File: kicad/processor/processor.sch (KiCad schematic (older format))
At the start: 24 parts, among them J1 CONN_02X07, U1 ESP32-WROOM, U2 BME280, U3 TCA9534A

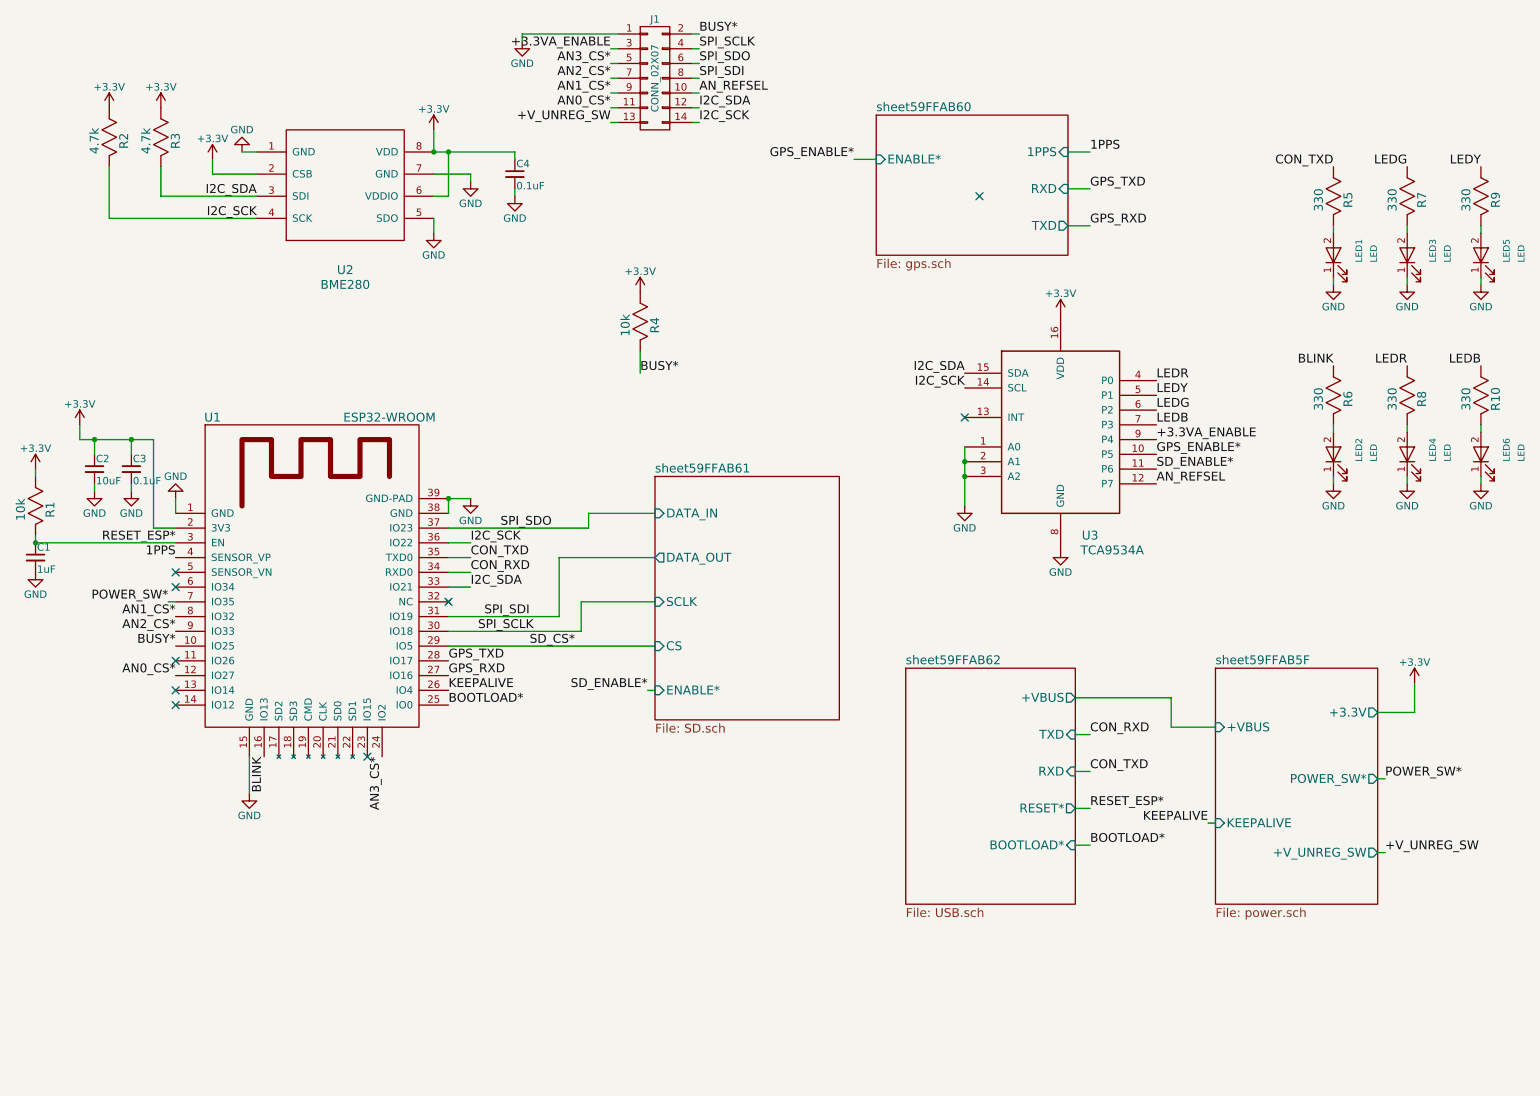
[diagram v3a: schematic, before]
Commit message: First cut layout power supply, fix netclasses, footprint for connector
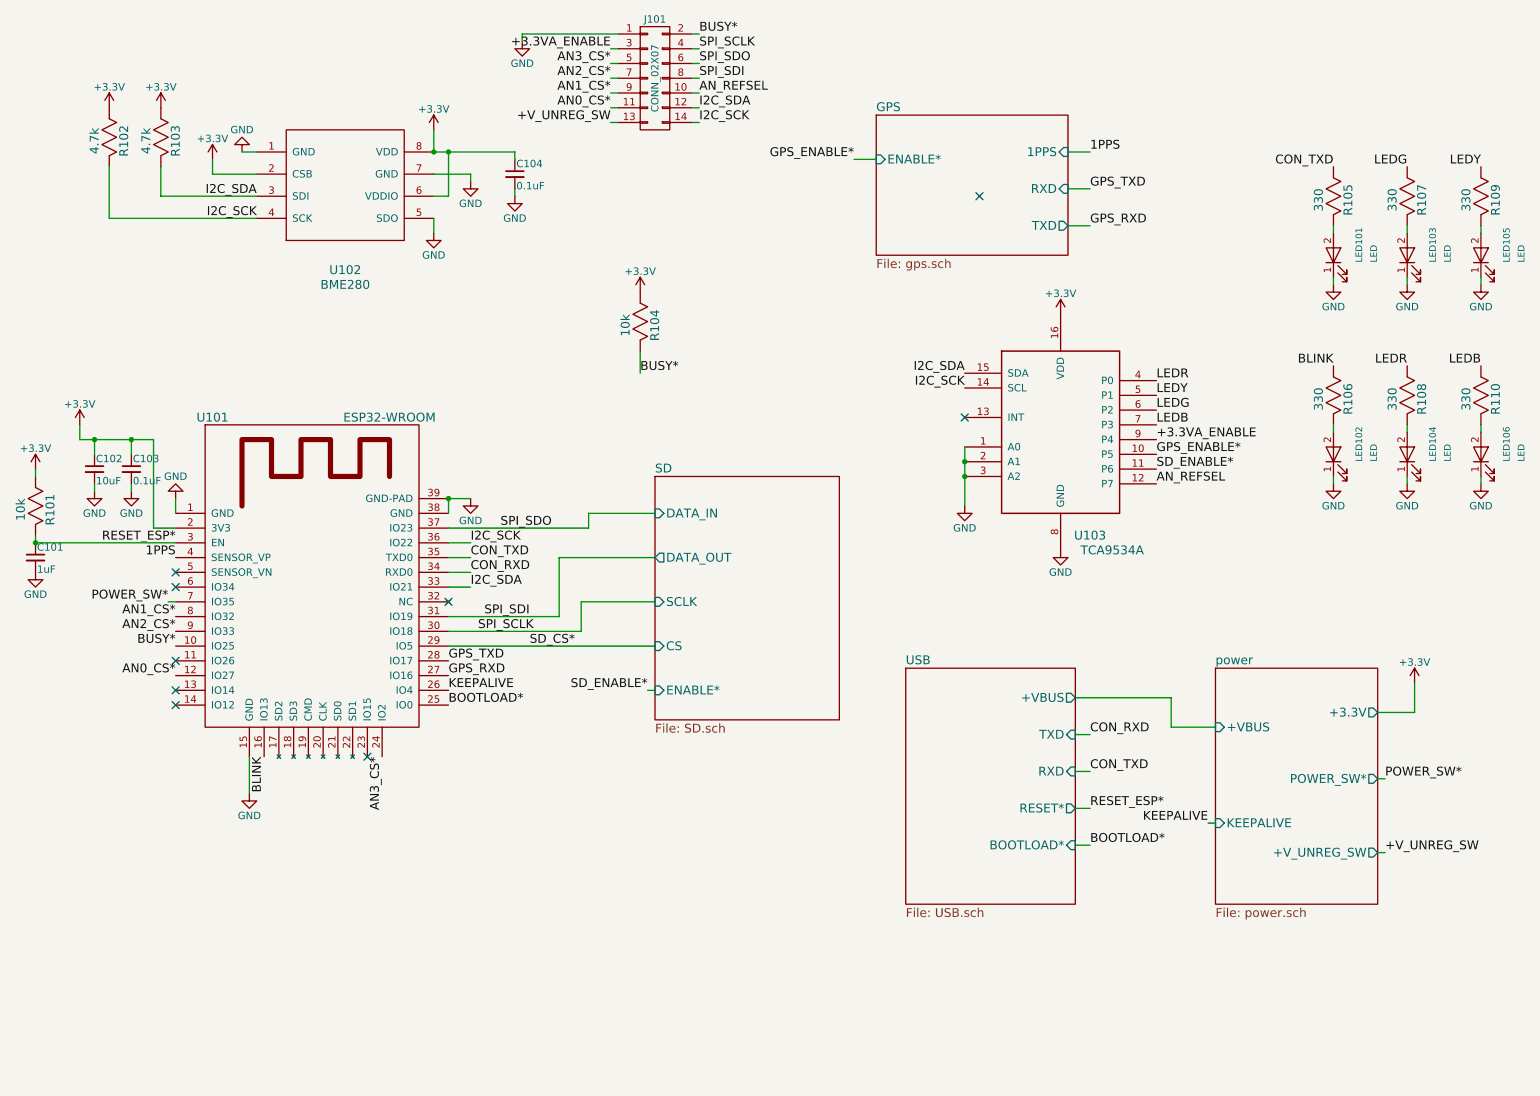
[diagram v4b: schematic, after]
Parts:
- J101: renamed from J1; footprint (none) -> paddle:conn_FCI_14
- renumbered C1 to C101, C2 to C102, C3 to C103, C4 to C104, LED1 to LED101, LED2 to LED102, LED3 to LED103, LED4 to LED104, LED5 to LED105, LED6 to LED106, R1 to R101, R2 to R102, R3 to R103, R4 to R104, R5 to R105, R6 to R106, R7 to R107, R8 to R108, R9 to R109, R10 to R110, U1 to U101, U2 to U102, U3 to U103
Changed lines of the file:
@@
 $EndDescr
 $Comp
-L R_US R4
+L R_US R104
 U 1 1 59CCA424
 P 4300 2550
-F 0 "R4" H 4325 2650 60  0000 C CNN
+F 0 "R104" H 4325 2650 60  0000 C CNN
 F 1 "10k" H 4325 2450 60  0000 C CNN
 F 2 "paddle:R_0603" H 4300 2200 60  0001 C CNN
@@
 	4650 1100 4700 1100
 $Comp
-L CONN_02X07 J1
+L CONN_02X07 J101
 U 1 1 59FE79E2
 P 4400 900
-F 0 "J1" H 4400 1300 50  0000 C CNN
+F 0 "J101" H 4400 1300 50  0000 C CNN
 F 1 "CONN_02X07" V 4400 900 50  0000 C CNN
-F 2 "" H 4400 -300 50  0001 C CNN
+F 2 "paddle:conn_FCI_14" H 4400 -300 50  0001 C CNN
 F 3 "" H 4400 -300 50  0001 C CNN
 	1    4400 900
@@
 NoConn ~ 3000 4450
 $Comp
-L C_Small C3
+L C_Small C103
 U 1 1 59FFAB7B
 P 850 3550
-F 0 "C3" H 860 3620 50  0000 L CNN
+F 0 "C103" H 860 3620 50  0000 L CNN
 F 1 "0.1uF" H 860 3470 50  0000 L CNN
 F 2 "paddle:SMD_0805" H 850 3550 50  0001 C CNN
@@
 $EndComp
 $Comp
-L C_Small C2
+L C_Small C102
 U 1 1 59FFAB88
 P 600 3550
-F 0 "C2" H 610 3620 50  0000 L CNN
+F 0 "C102" H 610 3620 50  0000 L CNN
 F 1 "10uF" H 610 3470 50  0000 L CNN
 F 2 "paddle:SMD_0805" H 600 3550 50  0001 C CNN
@@
 $EndComp
 $Comp
-L R_US R2
+L R_US R102
 U 1 1 59FFAB95
 P 700 1300
-F 0 "R2" H 725 1400 60  0000 C CNN
+F 0 "R102" H 725 1400 60  0000 C CNN
 F 1 "4.7k" H 725 1200 60  0000 C CNN
 F 2 "paddle:R_0603" H 700 950 60  0001 C CNN
@@
 $EndComp
 $Comp
-L R_US R3
+L R_US R103
 U 1 1 59FFAB9C
 P 1050 1300
-F 0 "R3" H 1075 1400 60  0000 C CNN
+F 0 "R103" H 1075 1400 60  0000 C CNN
 F 1 "4.7k" H 1075 1200 60  0000 C CNN
 F 2 "paddle:R_0603" H 1050 950 60  0001 C CNN
@@
 RESET_ESP*
 $Comp
-L C_Small C1
+L C_Small C101
 U 1 1 59FFABB1
 P 200 4150
-F 0 "C1" H 210 4220 50  0000 L CNN
+F 0 "C101" H 210 4220 50  0000 L CNN
 F 1 "1uF" H 210 4070 50  0000 L CNN
 F 2 "paddle:SMD_0805" H 200 4150 50  0001 C CNN
@@
 $EndComp
 $Comp
-L R_US R1
+L R_US R101
 U 1 1 59FFABBE
 P 200 3800
-F 0 "R1" H 225 3900 60  0000 C CNN
+F 0 "R101" H 225 3900 60  0000 C CNN
 F 1 "10k" H 225 3700 60  0000 C CNN
 F 2 "paddle:R_0603" H 200 3450 60  0001 C CNN
@@
 S 8200 4900 1100 1600
 U 59FFABEE
-F0 "sheet59FFAB5F" 60
+F0 "power" 60
 F1 "power.sch" 60
 F2 "KEEPALIVE" I L 8200 5950 60
@@
 $EndComp
 $Comp
-L LED LED3
+L LED LED103
 U 1 1 59FFAC1A
 P 9500 2100
-F 0 "LED3" H 9450 1900 45  0000 L BNN
+F 0 "LED103" H 9450 1900 45  0000 L BNN
 F 1 "LED" H 9450 1800 45  0000 L BNN
 F 2 "paddle:SMD_D_0805" H 9300 2130 20  0001 C CNN
@@
 $EndComp
 $Comp
-L R_US R7
+L R_US R107
 U 1 1 59FFAC21
 P 9500 1700
-F 0 "R7" H 9525 1800 60  0000 C CNN
+F 0 "R107" H 9525 1800 60  0000 C CNN
 F 1 "330" H 9525 1600 60  0000 C CNN
 F 2 "paddle:R_0603" H 9500 1350 60  0001 C CNN
@@
 $EndComp
 $Comp
-L LED LED5
+L LED LED105
 U 1 1 59FFAC28
 P 10000 2100
-F 0 "LED5" H 9950 1900 45  0000 L BNN
+F 0 "LED105" H 9950 1900 45  0000 L BNN
 F 1 "LED" H 9950 1800 45  0000 L BNN
 F 2 "paddle:SMD_D_0805" H 9800 2130 20  0001 C CNN
@@
 $EndComp
 $Comp
-L LED LED4
+L LED LED104
 U 1 1 59FFAC2F
 P 9500 3450
-F 0 "LED4" H 9450 3250 45  0000 L BNN
+F 0 "LED104" H 9450 3250 45  0000 L BNN
 F 1 "LED" H 9450 3150 45  0000 L BNN
 F 2 "paddle:SMD_D_0805" H 9300 3480 20  0001 C CNN
@@
 $EndComp
 $Comp
-L R_US R8
+L R_US R108
 U 1 1 59FFAC36
 P 9500 3050
-F 0 "R8" H 9525 3150 60  0000 C CNN
+F 0 "R108" H 9525 3150 60  0000 C CNN
 F 1 "330" H 9525 2950 60  0000 C CNN
 F 2 "paddle:R_0603" H 9500 2700 60  0001 C CNN
@@
 $EndComp
 $Comp
-L LED LED6
+L LED LED106
 U 1 1 59FFAC3D
 P 10000 3450
-F 0 "LED6" H 9950 3250 45  0000 L BNN
+F 0 "LED106" H 9950 3250 45  0000 L BNN
 F 1 "LED" H 9950 3150 45  0000 L BNN
 F 2 "paddle:SMD_D_0805" H 9800 3480 20  0001 C CNN
@@
 $EndComp
 $Comp
-L R_US R10
+L R_US R110
 U 1 1 59FFAC44
 P 10000 3050
-F 0 "R10" H 10025 3150 60  0000 C CNN
+F 0 "R110" H 10025 3150 60  0000 C CNN
 F 1 "330" H 10025 2950 60  0000 C CNN
 F 2 "paddle:R_0603" H 10000 2700 60  0001 C CNN
@@
 S 5900 1150 1300 950
 U 59FFAC69
-F0 "sheet59FFAB60" 60
+F0 "GPS" 60
 F1 "gps.sch" 60
 F2 "1PPS" I R 7200 1400 60
@@
 S 4400 3600 1250 1650
 U 59FFAC84
-F0 "sheet59FFAB61" 60
+F0 "SD" 60
 F1 "SD.sch" 60
 F2 "DATA_OUT" O L 4400 4150 60
@@
 +V_UNREG_SW
 $Comp
-L TCA9534A U3
+L TCA9534A U103
 U 1 1 59FFAC9F
 P 7150 3300
-F 0 "U3" H 7350 2600 60  0000 C CNN
+F 0 "U103" H 7350 2600 60  0000 C CNN
 F 1 "TCA9534A" H 7500 2500 60  0000 C CNN
 F 2 "paddle:TSSOP-16-1EP_4.4x5mm_Pitch0.65mm" H 7150 2500 60  0001 C CNN
@@
 NoConn ~ 6500 3200
 $Comp
-L R_US R9
+L R_US R109
 U 1 1 59FFACB0
 P 10000 1700
-F 0 "R9" H 10025 1800 60  0000 C CNN
+F 0 "R109" H 10025 1800 60  0000 C CNN
 F 1 "330" H 10025 1600 60  0000 C CNN
 F 2 "paddle:R_0603" H 10000 1350 60  0001 C CNN
@@
 Connection ~ 3000 3750
 $Comp
-L LED LED1
+L LED LED101
 U 1 1 59FFAD10
 P 9000 2100
-F 0 "LED1" H 8950 1900 45  0000 L BNN
+F 0 "LED101" H 8950 1900 45  0000 L BNN
 F 1 "LED" H 8950 1800 45  0000 L BNN
 F 2 "paddle:SMD_D_0805" H 8800 2130 20  0001 C CNN
@@
 $EndComp
 $Comp
-L R_US R5
+L R_US R105
 U 1 1 59FFAD17
 P 9000 1700
-F 0 "R5" H 9025 1800 60  0000 C CNN
+F 0 "R105" H 9025 1800 60  0000 C CNN
 F 1 "330" H 9025 1600 60  0000 C CNN
 F 2 "paddle:R_0603" H 9000 1350 60  0001 C CNN
@@
 	700  1850 1700 1850
 $Comp
-L LED LED2
+L LED LED102
 U 1 1 59FFAD29
 P 9000 3450
-F 0 "LED2" H 8950 3250 45  0000 L BNN
+F 0 "LED102" H 8950 3250 45  0000 L BNN
 F 1 "LED" H 8950 3150 45  0000 L BNN
 F 2 "paddle:SMD_D_0805" H 8800 3480 20  0001 C CNN
@@
 $EndComp
 $Comp
-L R_US R6
+L R_US R106
 U 1 1 59FFAD30
 P 9000 3050
-F 0 "R6" H 9025 3150 60  0000 C CNN
+F 0 "R106" H 9025 3150 60  0000 C CNN
 F 1 "330" H 9025 2950 60  0000 C CNN
 F 2 "paddle:R_0603" H 9000 2700 60  0001 C CNN
@@
 S 6100 4900 1150 1600
 U 59FFAD44
-F0 "sheet59FFAB62" 60
+F0 "USB" 60
 F1 "USB.sch" 60
 F2 "BOOTLOAD*" I R 7250 6100 60
@@
 	7250 6100 7350 6100
 $Comp
-L BME280 U2
+L BME280 U102
 U 1 1 59FFAD60
 P 2300 1650
-F 0 "U2" H 2300 1100 60  0000 C CNN
+F 0 "U102" H 2300 1100 60  0000 C CNN
 F 1 "BME280" H 2300 1000 60  0000 C CNN
 F 2 "paddle:BME280" H 1975 1200 60  0001 C CNN
@@
 $EndComp
 $Comp
-L C_Small C4
+L C_Small C104
 U 1 1 59FFAD67
 P 3450 1550
-F 0 "C4" H 3460 1620 50  0000 L CNN
+F 0 "C104" H 3460 1620 50  0000 L CNN
 F 1 "0.1uF" H 3460 1470 50  0000 L CNN
 F 2 "paddle:SMD_0805" H 3450 1550 50  0001 C CNN
@@
 	1150 3750 1150 3850
 $Comp
-L ESP32-WROOM U1
+L ESP32-WROOM U101
 U 1 1 59FFACB8
 P 2100 4450
-F 0 "U1" H 1400 5700 60  0000 C CNN
+F 0 "U101" H 1400 5700 60  0000 C CNN
 F 1 "ESP32-WROOM" H 2600 5700 60  0000 C CNN
 F 2 "paddle:ESP32-WROOM" H 2450 5800 60  0001 C CNN

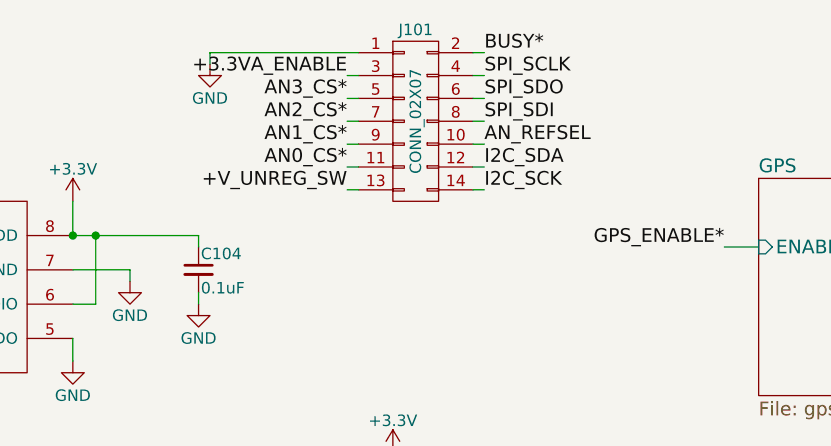
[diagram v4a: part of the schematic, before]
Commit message: Processor board routed, conn_FCI_14 switched to no hole version, port expander package fixed
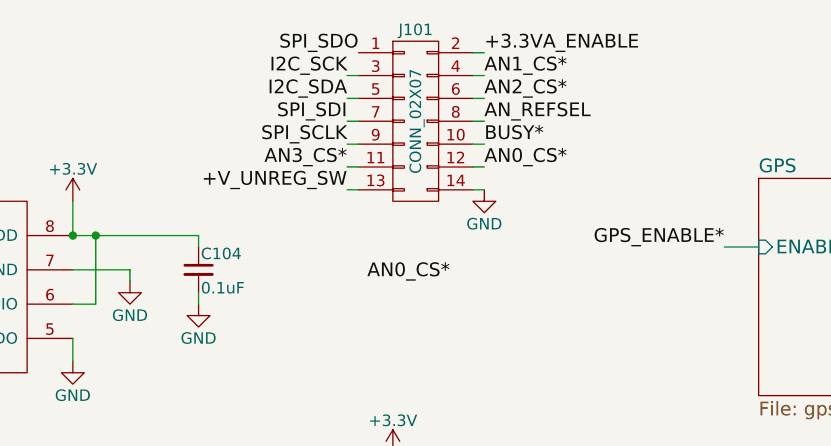
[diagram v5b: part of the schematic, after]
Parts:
- U103: footprint paddle:TSSOP-16-1EP_4.4x5mm_Pitch0.65mm -> paddle:SOIC-16
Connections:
- net +3.3VA_ENABLE: now also J101.2 (P2); no longer J101.3 (P3)
- net AN0_CS*: now also J101.12 (P12); no longer J101.11 (P11)
- net AN1_CS*: now also J101.4 (P4); no longer J101.9 (P9)
- net AN2_CS*: now also J101.6 (P6); no longer J101.7 (P7)
- net AN3_CS*: now also J101.11 (P11); no longer J101.5 (P5)
- net AN_REFSEL: now also J101.8 (P8); no longer J101.10 (P10)
- net BUSY*: now also J101.10 (P10); no longer J101.2 (P2)
- net GND: now also J101.14 (P14); no longer J101.1 (P1)
- net I2C_SCK: now also J101.3 (P3); no longer J101.14 (P14)
- net I2C_SDA: now also J101.5 (P5); no longer J101.12 (P12)
- net SPI_SCLK: now also J101.9 (P9); no longer J101.4 (P4)
- net SPI_SDI: now also J101.7 (P7); no longer J101.8 (P8)
- net SPI_SDO: now also J101.1 (P1); no longer J101.6 (P6)
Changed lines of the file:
@@
 Wire Wire Line
 	4300 2900 4300 2750
-Text Label 4700 600  0    60   ~ 0
+Text Label 4700 1000 0    60   ~ 0
 BUSY*
-Text Label 4700 700  0    60   ~ 0
+Text Label 4100 1000 2    60   ~ 0
 SPI_SCLK
-Text Label 4700 800  0    60   ~ 0
+Text Label 4150 600  2    60   ~ 0
 SPI_SDO
-Text Label 4700 900  0    60   ~ 0
+Text Label 4100 900  2    60   ~ 0
 SPI_SDI
 $Comp
 L GND #PWR02
 U 1 1 59FE79CA
-P 3500 650
-F 0 "#PWR02" H 3500 400 50  0001 C CNN
-F 1 "GND" H 3500 500 50  0000 C CNN
-F 2 "" H 3500 650 50  0001 C CNN
-F 3 "" H 3500 650 50  0001 C CNN
-	1    3500 650
-	1    0    0    -1
-$EndComp
-Text Label 4100 700  2    60   ~ 0
+P 4700 1200
+F 0 "#PWR02" H 4700 950 50  0001 C CNN
+F 1 "GND" H 4700 1050 50  0000 C CNN
+F 2 "" H 4700 1200 50  0001 C CNN
+F 3 "" H 4700 1200 50  0001 C CNN
+	1    4700 1200
+	1    0    0    -1
+$EndComp
+Text Label 4700 600  0    60   ~ 0
 +3.3VA_ENABLE
 Wire Wire Line
@@
 Wire Wire Line
 	4650 800  4700 800
-Wire Wire Line
-	4650 900  4700 900
-Wire Wire Line
-	4150 600  3500 600
-Wire Wire Line
-	3500 600  3500 650
 Wire Wire Line
 	4100 700  4150 700
@@
 +V_UNREG_SW
 Wire Wire Line
-	4650 1100 4700 1100
+	4650 1000 4700 1000
 $Comp
 L CONN_02X07 J101
@@
 F 0 "U103" H 7350 2600 60  0000 C CNN
 F 1 "TCA9534A" H 7500 2500 60  0000 C CNN
-F 2 "paddle:TSSOP-16-1EP_4.4x5mm_Pitch0.65mm" H 7150 2500 60  0001 C CNN
+F 2 "paddle:SOIC-16" H 7150 2500 60  0001 C CNN
 F 3 "" H 7150 2500 60  0001 C CNN
 	1    7150 3300
@@
 Text Label 1150 4750 2    60   ~ 0
 BUSY*
-Text Label 4700 1000 0    60   ~ 0
+Text Label 4700 900  0    60   ~ 0
 AN_REFSEL
 Wire Wire Line
-	4700 1000 4650 1000
-Text Label 4700 1100 0    60   ~ 0
+	4700 900  4650 900
+Text Label 4100 800  2    60   ~ 0
 I2C_SDA
-Text Label 4700 1200 0    60   ~ 0
+Text Label 4100 700  2    60   ~ 0
 I2C_SCK
 Text Label 3200 4650 0    60   ~ 0
@@
 Text Label 7350 5600 0    60   ~ 0
 CON_TXD
-Text Label 4100 800  2    60   ~ 0
+Text Label 4100 1100 2    60   ~ 0
 AN3_CS*
-Text Label 4100 900  2    60   ~ 0
-AN2_CS*
-Text Label 4100 1100 2    60   ~ 0
+Text Label 4550 1600 2    60   ~ 0
 AN0_CS*
 Text Label 5750 1450 2    60   ~ 0
@@
 Text Label 2550 5500 3    60   ~ 0
 AN3_CS*
-Text Label 4100 1000 2    60   ~ 0
+Text Label 4700 700  0    60   ~ 0
 AN1_CS*
 Text Label 1150 4950 2    60   ~ 0
@@
 NoConn ~ 1150 4850
 NoConn ~ 6600 1700
+Text Label 4700 1100 0    60   ~ 0
+AN0_CS*
+Text Label 4700 800  0    60   ~ 0
+AN2_CS*
+Wire Wire Line
+	4700 1100 4650 1100
 $EndSCHEMATC
